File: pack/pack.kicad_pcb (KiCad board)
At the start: 2 copper layers, 48 x 28.2 mm, 8 parts

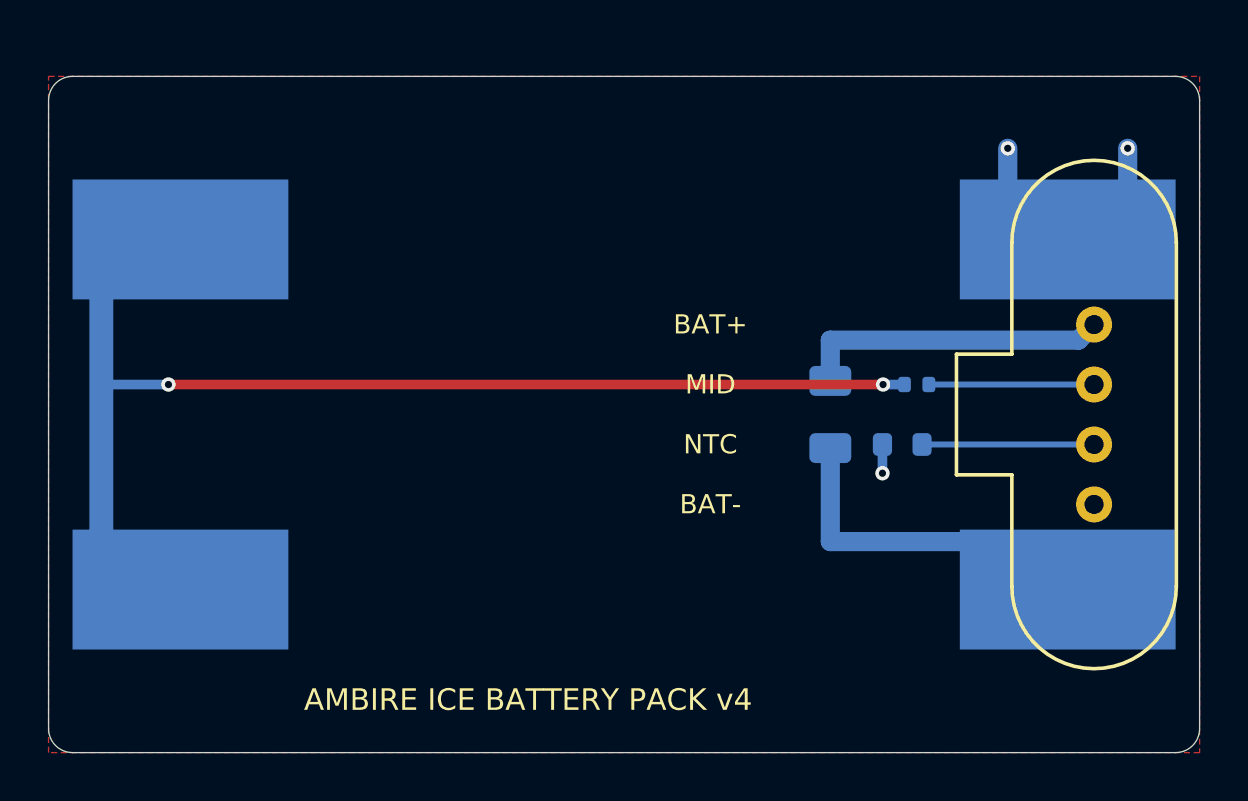
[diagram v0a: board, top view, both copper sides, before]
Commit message: v4 device board: the pack's magnetic receptacle south of the MCU, routed, DRC clean; pack and case to match
Schematic (src/blocks/Power.tsx): the cell clips out, Xinyangze's 4-pin magnetic
receptacle YZ103915020T-04025-02 (C6276862) in (BAT, CELL_MID, CHG_TS, BAT_N); the
board's thermistor out (the pack carries it); a 1M/1M divider and 100 nF read the
pack's mid-point on PA6; the BQ25172 set for two cells (VSET 36k) and fed from VBUS
(a full two-cell pack leaves too little headroom under 3.3 V); its hold-off pull-up
stays on the USB 3.3 V rail (5 V would exceed PB0's rating with the MCU unpowered).
AIRGAP_SENSE PE7 -> PB15 and CHG_STAT PE8 -> PA3: the receptacle sends the display
lines' fan across the MCU's south side. checkNets, checkMcuAf: ok.

Land (board/wallet.pretty): the receptacle from the maker's drawing (2015-07-08): 4 x
2.2 mm pads at 2.54, slots for its two 5.0 x 1.5 x 0.5 bosses (taken flush with the long
edges: to check on a sample), bare copper under its magnets; 2.2 mm mounted (2.0 on
0.2 feet; the case had 2.0). U8 gets its own SOT-23-6 copy without the silk side that
lands on the display connector's tab.

Placement: the receptacle east-west at (22.0, 42.28) in the old channel south of the
MCU (the east side is the touch tail's lane: an earlier layout put it on the tail); the
TFT connector 5.5 mm south and its slot 2.5 mm (tail slack 3.0 mm, checkFpc's limit;
the slot keeps 0.36 mm to the radio module's pads); the VDD11 decap turned along the
MCU's edge; displaced: R_AIRS, the display's two decaps, U8 (turned) and C_RCT, the
charger switch (Q_CHG, R_CHGHI, R_ISETH). placementScan: the same findings as before.

Routing: the changed region ripped locally and rebuilt with humanizedKicadAutoRouter
(keep-copper), then by hand: RADIO_RX/TX through the lane between the radio module's
pad rows (the slot walled off their north exits), U11.21's GND tie north to a via
(none in its pad), AIRGAP's approach to U6 north of its GND pad, owner-style ties for
C_NOR.2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
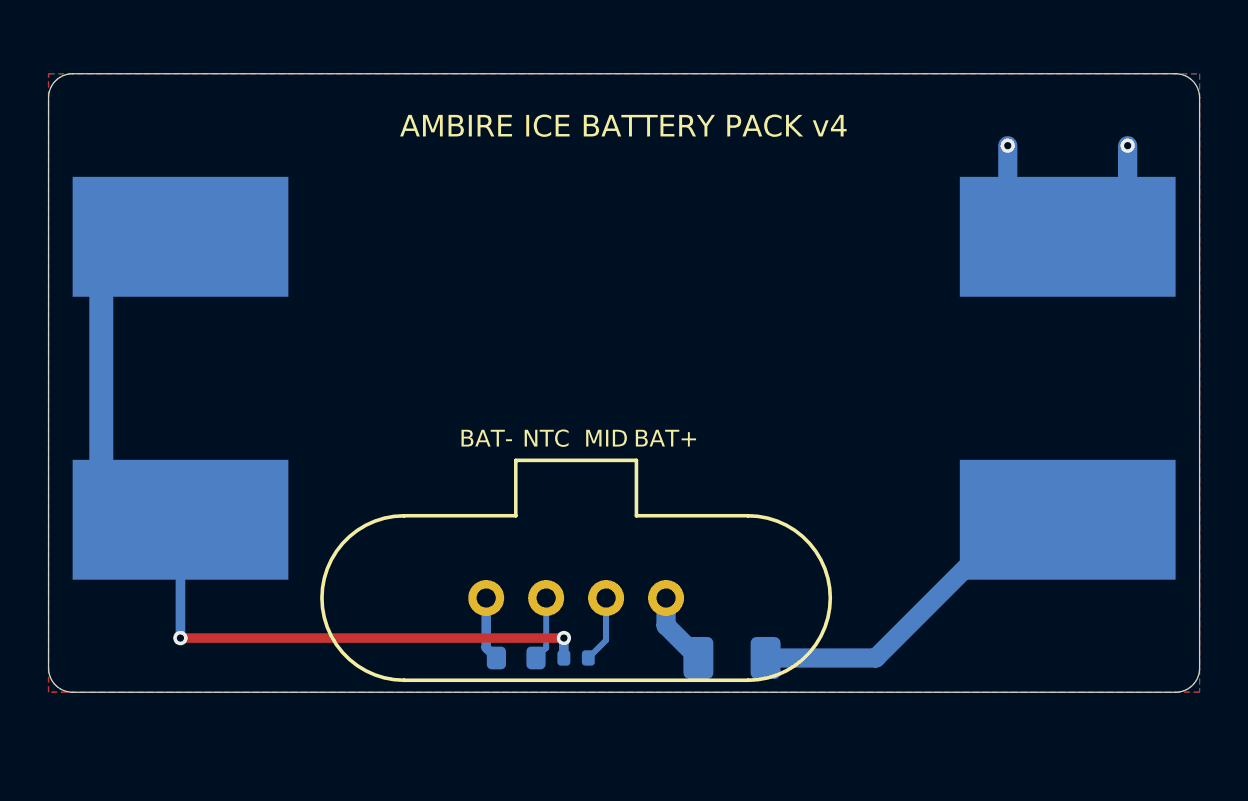
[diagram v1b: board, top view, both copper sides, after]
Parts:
- moved J_PACK 22.9 mm to (22.0, 42.3), turned to 180 degrees
- moved RT_PACK 18.4 mm to (19.5, 44.8)
- moved R_MID 18.2 mm to (22.0, 44.8)
- moved F_BAT 10.9 mm to (28.5, 44.8), turned to 0 degrees
- moved BT_N2 2.91 mm to (5.50, 39.0)
- moved BT_P2 2.91 mm to (42.5, 39.0)
- moved BT_N1 0.11 mm to (42.5, 27.2)
- moved BT_P1 0.11 mm to (5.50, 27.2)
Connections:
- F_BAT pad 1: CELL+ -> BAT+
- F_BAT pad 2: BAT+ -> CELL+
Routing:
- net MID: track 44.1 -> 27.6 mm
- net BAT+: track 13.0 -> 3.06 mm
- net NTC: track 7.18 -> 2.68 mm
- net MID_SENSE: track 6.89 -> 2.81 mm
- net BAT-: track 4.80 -> 6.28 mm, vias 3 -> 2
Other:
- board size 48 x 28.2 mm -> 48 x 25.8 mm

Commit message: v4 pack: the cells 12.8 mm apart (was 11.8): a cell going in must not short the neighbouring clip
A cell goes into its MYOUNG clips through the arms' tips, 6.9 mm apart in the clip's
model: each arm swings out ~1.7 mm at its tip and ~0.9 mm at its widest (hinging at its
root). At 11.8 mm (courtyards touching) the neighbouring arms were 0.8 mm apart, and on
the east side they are the pack's minus and the south cell's plus, ahead of the fuse:
an arm swinging out while a cell went in could short the whole pack. generate.py now
spaces the cells by the arms' span plus ARM_GAP = twice that swing (1.8 mm): 12.8 mm.

Pack 51.2 x 29.2 mm (was 28.6), its board 48.0 x 26.4; the male's joints 0.47 mm under
the south cell's can (the check wants 0.3). The device board is unchanged (the
receptacle stays put). makePack.py takes the clips from enclosure/pack_clips.kicad_pcb
(the device board no longer has them; the earlier pack rebuild had read them from the
board before v4 removed them). Pack board: DRC nothing, as saved and refilled;
cleanCopper clean; order set and renders regenerated. Case (tray) and page regenerated.

Co-Authored-By: Claude Opus 5.5 <noreply@anthropic.com>
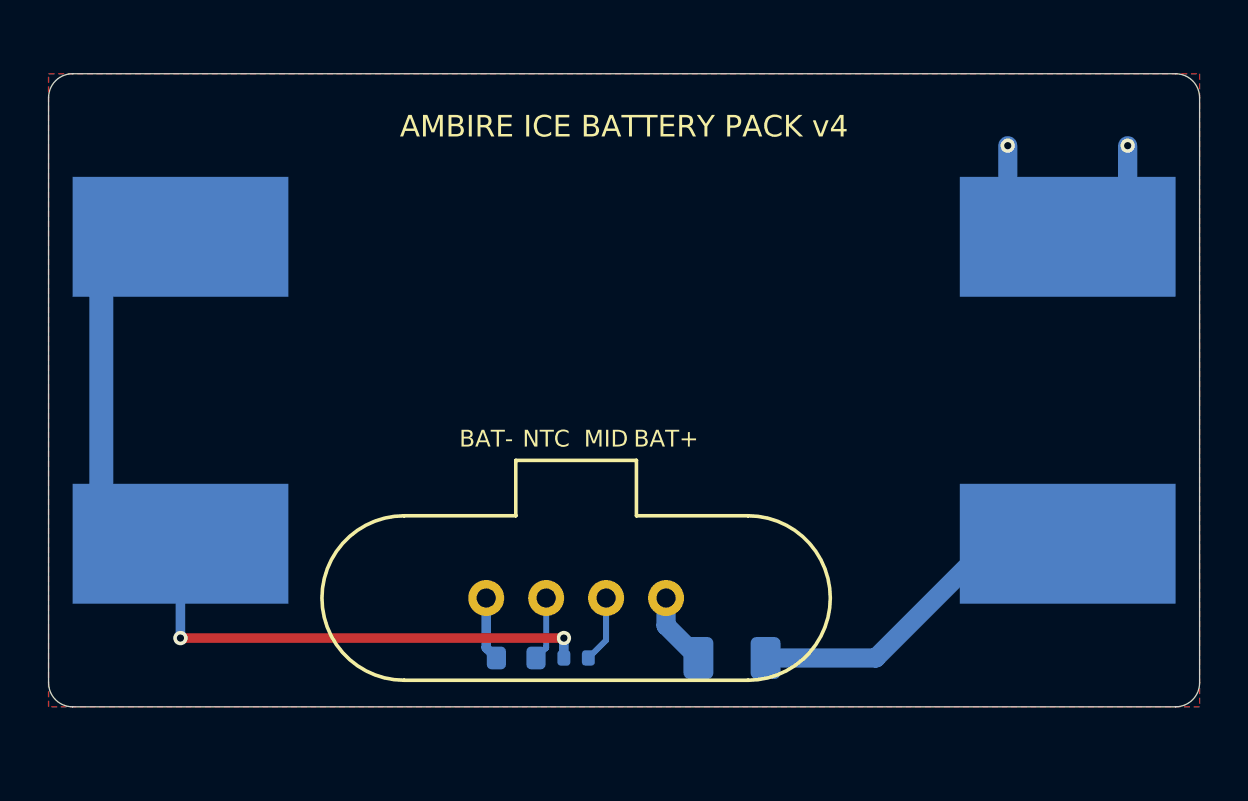
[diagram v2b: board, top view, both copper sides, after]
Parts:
- moved BT_N2 1.00 mm to (5.50, 40.0)
- moved BT_P2 1.00 mm to (42.5, 40.0)
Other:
- board size 48 x 25.8 mm -> 48 x 26.4 mm

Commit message: Pack board rebuilt for the closer pack; boost caps' derating from Samsung's curve
The pack now sits 1.5 mm closer to the device, so the camera's cone lets it
1.05 mm further north: pack/makePack.py rebuilt the board from the case's
numbers (DRC clean, pin order unchanged), pack order set recut. The boost caps
keep ~20 uF each at 3.3 V by Samsung's DC-bias curve (-57 %), over the 22 uF the
LTC3539 needs even at -20 % and 85 C.

Co-Authored-By: Claude Opus 5.5 <noreply@anthropic.com>
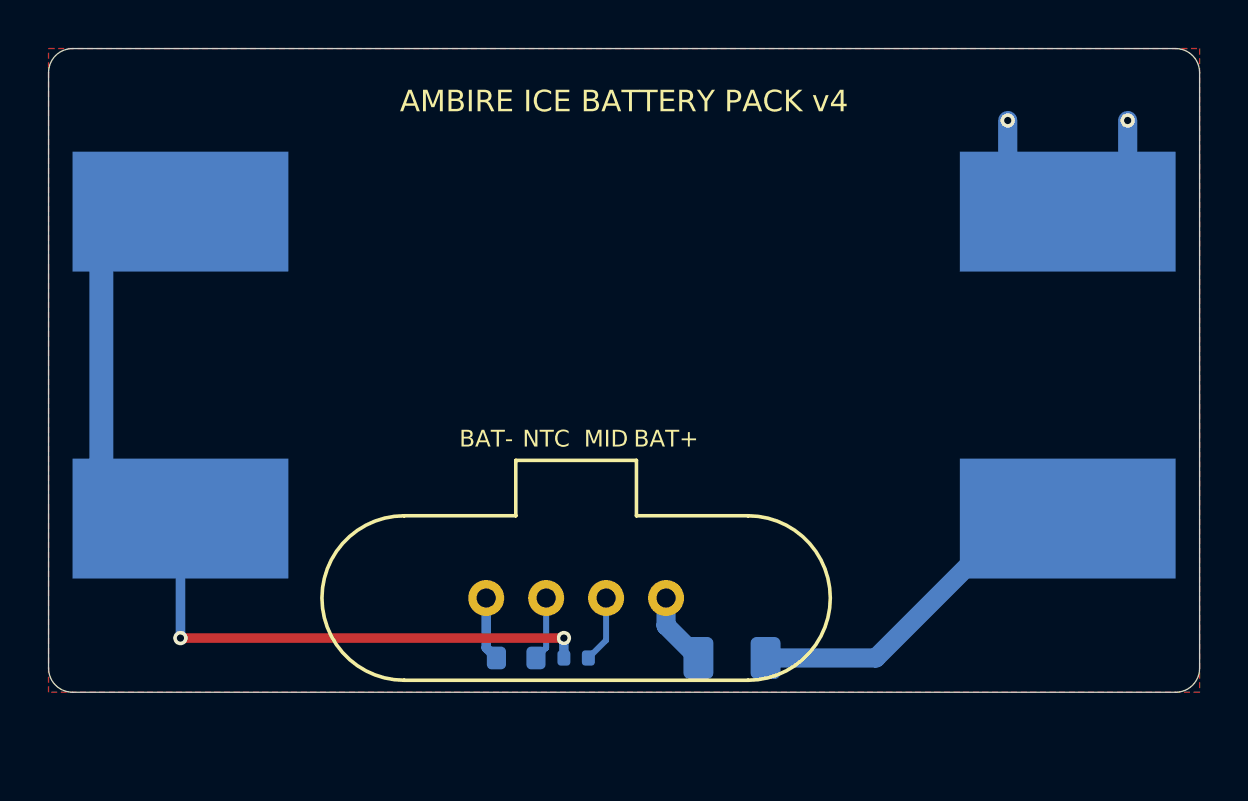
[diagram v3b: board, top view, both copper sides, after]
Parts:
- moved BT_N2 1.05 mm to (5.50, 39.0)
- moved BT_P2 1.05 mm to (42.5, 39.0)
- moved BT_N1 1.05 mm to (42.5, 26.2)
- moved BT_P1 1.05 mm to (5.50, 26.2)
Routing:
- net MID: track 27.6 -> 28.6 mm
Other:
- board size 48 x 26.4 mm -> 48 x 26.8 mm
